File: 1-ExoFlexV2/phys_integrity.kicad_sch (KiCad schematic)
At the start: 18 parts, among them J112 Jumper, J113 Jumper, J114 Jumper, J115 Jumper, J116 Jumper, J117 Jumper, U88 OR Gate, U89 OR Gate, U90 OR Gate, U91 OR Gate, U92 OR Gate

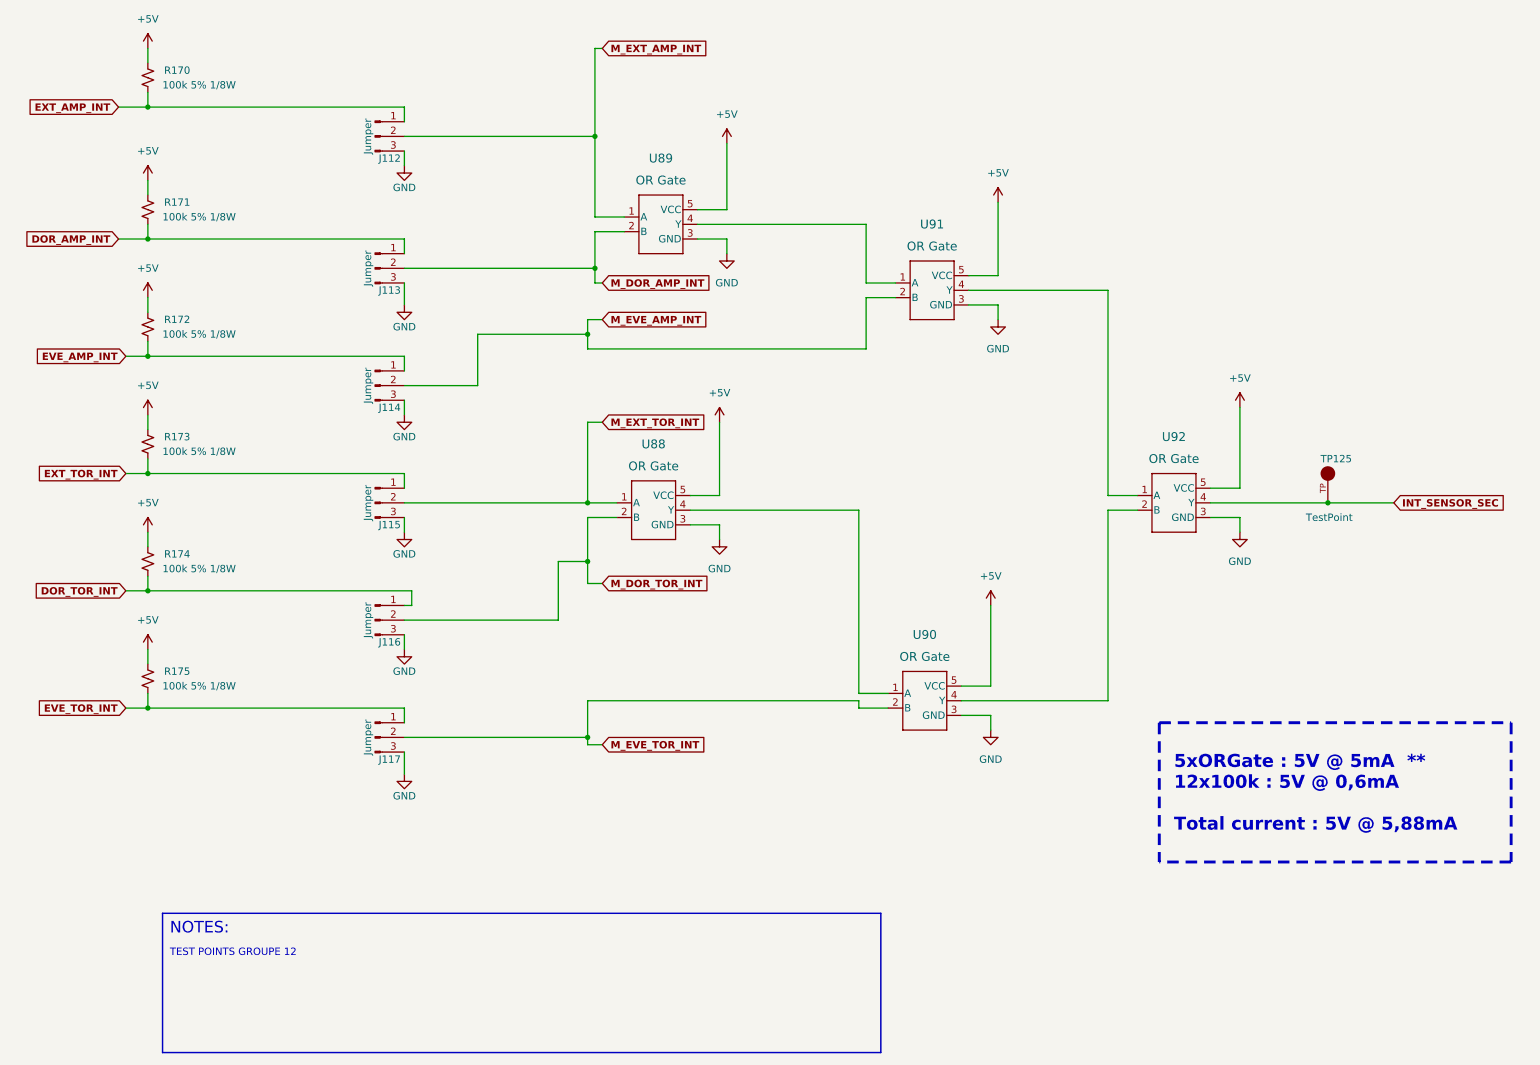
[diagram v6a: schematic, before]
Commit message: Finalisation schéma FIN
- Changement des uméro pour les inverseurs
- Changement des connecteur et début de placement
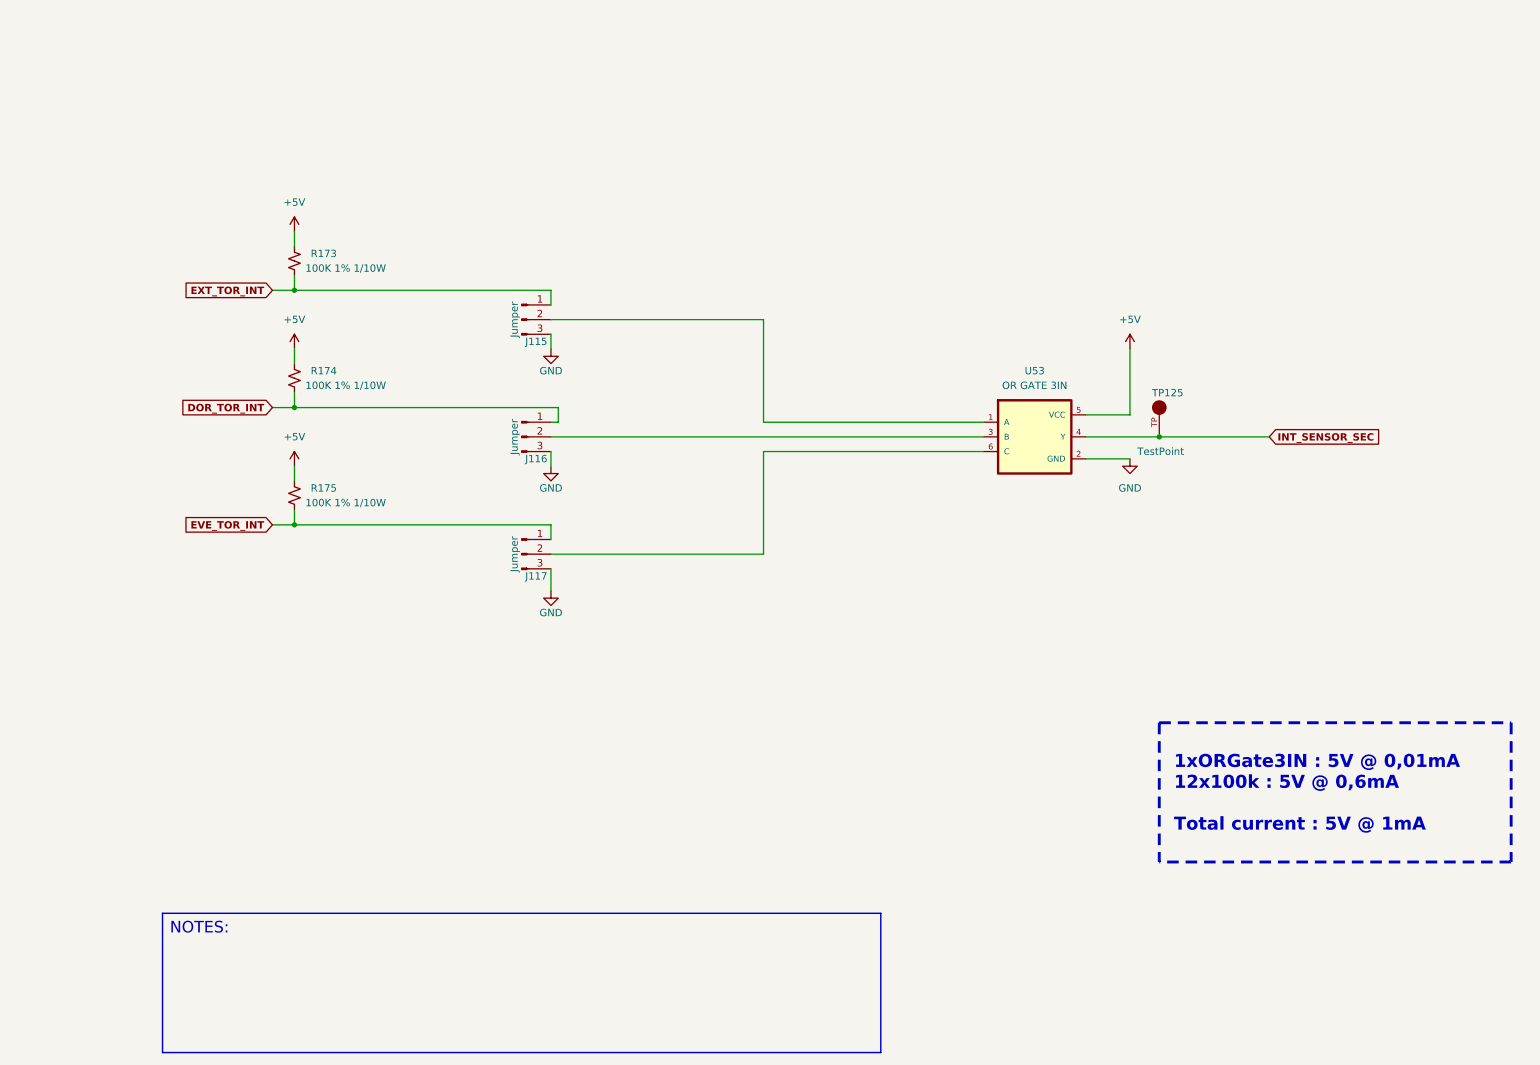
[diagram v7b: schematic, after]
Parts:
- removed J112, J113, J114: Jumper, Connector_PinHeader_2.54mm:PinHeader_1x03_P2.54mm_Vertical, symbol Connector:Conn_01x03_Male
- removed R170, R171, R172: 100k 5% 1/8W, Resistor_SMD:R_0805_2012Metric, symbol Device:R_Small_US
- removed U88, U89, U90, U91, U92: OR Gate, FootPrint:SOT95P270X145-5N, symbol SymLib:SN74LVC1G32DBVR
- added U53: OR GATE 3IN, FootPrintLib:SOT95P280X145-6N, symbol SymLib:SN74LVC1G332DBVR
- R173, R174, R175: value 100k 5% 1/8W -> 100K 1% 1/10W; footprint Resistor_SMD:R_0805_2012Metric -> Resistor_SMD:R_0603_1608Metric; DESCRIPTION 100 kOhms ±5% 0.125W, 1/8W Chip Resistor 0805 (2012 Metric)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 -> 100 kOhms ±1% 0.1W, 1/10W Chip Resistor 0603 (1608 Metric) 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; PACKAGE 0805 (2012 Metric) -> 0603 (1608 Metric); PART NUMBER ERJ-6GEYJ104V -> ERJ-3EKF1003V
- TP125: NOTES (none) -> DO NOT POPULATE; PURCHASE-URL https://pricing.snapeda.com/search/part/5005/?ref=eda -> (none)
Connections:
- net +5V: now also U53.5 (VCC)
- net GND: now also U53.2 (GND)
- net INT_SENSOR_SEC: now also U53.4 (Y)
- net M_DOR_TOR_INT: no longer names the net of J116.2 (Pin_2)
- net M_DOR_TOR_INT: now also U53.3 (B)
- net M_EVE_TOR_INT: no longer names the net of J117.2 (Pin_2)
- net M_EVE_TOR_INT: now also U53.6 (C)
- net M_EXT_TOR_INT: no longer names the net of J115.2 (Pin_2)
- net M_EXT_TOR_INT: now also U53.1 (A)
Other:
- note added: "1xORGate3IN : 5V @ 0,01mA 12x100k : 5V @ 0,6mA Total current : 5V @ 1mA"
- note removed: "5xORGate : 5V @ 5mA ** 12x100k : 5V @ 0,6mA Total current : 5V @ 5,88mA"
- note removed: "TEST POINTS GROUPE 12"
- moved on the sheet: J115, J116, J117, R173, R174, R175, TP125

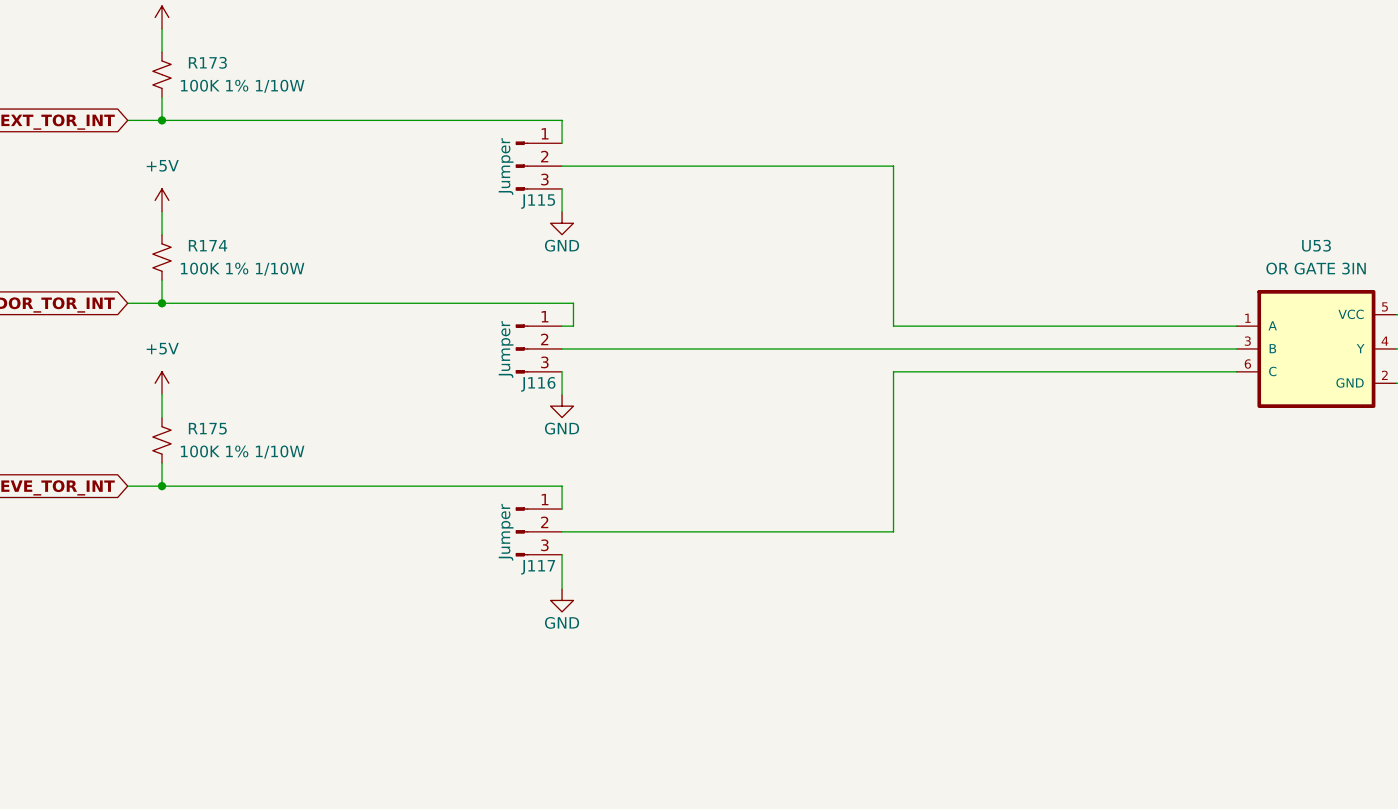
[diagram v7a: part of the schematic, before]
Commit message: Routage pour Review 1
- Replacement des test point pour faciliter le rework
- Correction des erreurs dans le BOM
-
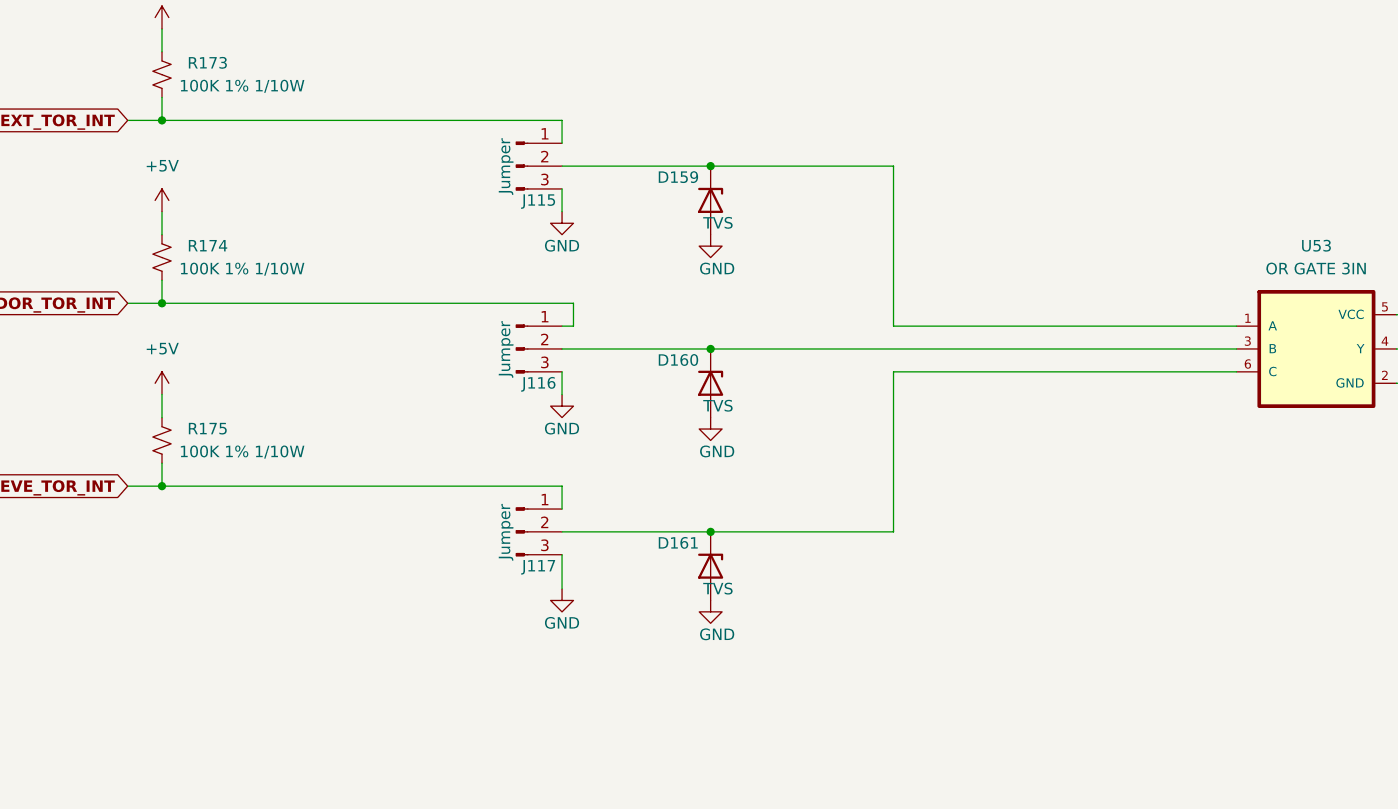
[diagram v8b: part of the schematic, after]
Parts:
- added D159, D160, D161: TVS, FootPrint:DPY2_TEX, symbol Device:D_Zener
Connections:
- net GND: now also D159.2 (A), D160.2 (A), D161.2 (A)
- net at J117.2 (Pin_2), U53.6 (C): now also D161.1 (K)
- net at J115.2 (Pin_2), U53.1 (A): now also D159.1 (K)
- net at J116.2 (Pin_2), U53.3 (B): now also D160.1 (K)
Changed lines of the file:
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@@
   (junction (at 71.12 102.87) (diameter 0) (color 0 0 0 0)
   )
+  (junction (at 132.08 107.95) (diameter 0) (color 0 0 0 0)
+  )
+  (junction (at 132.08 87.63) (diameter 0) (color 0 0 0 0)
+  )
+  (junction (at 132.08 67.31) (diameter 0) (color 0 0 0 0)
+  )
   (junction (at 71.12 62.23) (diameter 0) (color 0 0 0 0)
   )
@@
   )
   (wire (pts (xy 152.4 90.17) (xy 190.5 90.17))
+    (stroke (width 0) (type default) (color 0 0 0 0))
+  )
+  (wire (pts (xy 132.08 107.95) (xy 152.4 107.95))
     (stroke (width 0) (type default) (color 0 0 0 0))
   )
@@
     (stroke (width 0) (type default) (color 0 0 0 0))
   )
-  (wire (pts (xy 116.84 82.55) (xy 71.12 82.55))
+  (wire (pts (xy 71.12 82.55) (xy 116.84 82.55))
     (stroke (width 0) (type default) (color 0 0 0 0))
   )
@@
     (stroke (width 0) (type default) (color 0 0 0 0))
   )
-  (wire (pts (xy 115.57 87.63) (xy 190.5 87.63))
+  (wire (pts (xy 115.57 87.63) (xy 132.08 87.63))
     (stroke (width 0) (type default) (color 0 0 0 0))
   )
@@
     (stroke (width 0) (type default) (color 0 0 0 0))
   )
+  (wire (pts (xy 71.12 102.87) (xy 115.57 102.87))
+    (stroke (width 0) (type default) (color 0 0 0 0))
+  )
   (wire (pts (xy 71.12 52.07) (xy 71.12 54.61))
     (stroke (width 0) (type default) (color 0 0 0 0))
   )
-  (wire (pts (xy 71.12 102.87) (xy 115.57 102.87))
+  (wire (pts (xy 132.08 67.31) (xy 152.4 67.31))
     (stroke (width 0) (type default) (color 0 0 0 0))
   )
@@
     (stroke (width 0) (type default) (color 0 0 0 0))
   )
-  (wire (pts (xy 115.57 67.31) (xy 152.4 67.31))
+  (wire (pts (xy 132.08 87.63) (xy 190.5 87.63))
+    (stroke (width 0) (type default) (color 0 0 0 0))
+  )
+  (wire (pts (xy 115.57 67.31) (xy 132.08 67.31))
     (stroke (width 0) (type default) (color 0 0 0 0))
   )
@@
     (stroke (width 0) (type default) (color 0 0 0 0))
   )
-  (wire (pts (xy 115.57 107.95) (xy 152.4 107.95))
+  (wire (pts (xy 115.57 107.95) (xy 132.08 107.95))
     (stroke (width 0) (type default) (color 0 0 0 0))
   )
@@
     (pin "2")
   )
+  (symbol (lib_id "power:GND") (at 132.08 95.25 0) (unit 1)
+    (in_bom yes) (on_board yes)
+    (property "Reference" "#PWR0618" (id 0) (at 132.08 101.6 0)
+      (effects (font (size 1.27 1.27)) hide)
+    )
+    (property "Value" "GND" (id 1) (at 130.81 99.06 0)
+      (effects (font (size 1.27 1.27)) (justify left))
+    )
+    (property "Footprint" "" (id 2) (at 132.08 95.25 0)
+      (effects (font (size 1.27 1.27)) hide)
+    )
+    (property "Datasheet" "" (id 3) (at 132.08 95.25 0)
+      (effects (font (size 1.27 1.27)) hide)
+    )
+    (pin "1")
+  )
+  (symbol (lib_id "power:GND") (at 132.08 115.57 0) (unit 1)
+    (in_bom yes) (on_board yes)
+    (property "Reference" "#PWR0619" (id 0) (at 132.08 121.92 0)
+      (effects (font (size 1.27 1.27)) hide)
+    )
+    (property "Value" "GND" (id 1) (at 130.81 119.38 0)
+      (effects (font (size 1.27 1.27)) (justify left))
+    )
+    (property "Footprint" "" (id 2) (at 132.08 115.57 0)
+      (effects (font (size 1.27 1.27)) hide)
+    )
+    (property "Datasheet" "" (id 3) (at 132.08 115.57 0)
+      (effects (font (size 1.27 1.27)) hide)
+    )
+    (pin "1")
+  )
+  (symbol (lib_id "Device:D_Zener") (at 132.08 111.76 270) (unit 1)
+    (in_bom yes) (on_board yes)
+    (property "Reference" "D161" (id 0) (at 130.81 109.22 90)
+      (effects (font (size 1.27 1.27)) (justify right))
+    )
+    (property "Value" "TVS" (id 1) (at 134.62 114.3 90)
+      (effects (font (size 1.27 1.27)) (justify right))
+    )
+    (property "Footprint" "FootPrint:DPY2_TEX" (id 2) (at 132.08 111.76 0)
+      (effects (font (size 1.27 1.27)) hide)
+    )
+    (property "Datasheet" "~" (id 3) (at 132.08 111.76 0)
+      (effects (font (size 1.27 1.27)) hide)
+    )
+    (property "DESCRIPTION" "TVS DIODE 5.5VWM 14VC 2X1SON" (id 4) (at 132.08 111.76 0)
+      (effects (font (size 1.27 1.27)) hide)
+    )
+    (property "MANUFACTURER" "Texas Instruments" (id 5) (at 132.08 111.76 0)
+      (effects (font (size 1.27 1.27)) hide)
+    )
+    (property "PACKAGE" "0402 (1006 Metric)" (id 6) (at 132.08 111.76 0)
+      (effects (font (size 1.27 1.27)) hide)
+    )
+    (property "PART NUMBER" "TPD1E05U06DPYR" (id 7) (at 132.08 111.76 0)
+      (effects (font (size 1.27 1.27)) hide)
+    )
+    (property "TYPE" "SMD" (id 8) (at 132.08 111.76 0)
+      (effects (font (size 1.27 1.27)) hide)
+    )
+    (pin "1")
+    (pin "2")
+  )
   (symbol (lib_id "Device:R_Small_US") (at 71.12 77.47 0) (unit 1)
     (in_bom yes) (on_board yes)
@@
     )
     (pin "1")
+  )
+  (symbol (lib_id "Device:D_Zener") (at 132.08 91.44 270) (unit 1)
+    (in_bom yes) (on_board yes)
+    (property "Reference" "D160" (id 0) (at 130.81 88.9 90)
+      (effects (font (size 1.27 1.27)) (justify right))
+    )
+    (property "Value" "TVS" (id 1) (at 134.62 93.98 90)
+      (effects (font (size 1.27 1.27)) (justify right))
+    )
+    (property "Footprint" "FootPrint:DPY2_TEX" (id 2) (at 132.08 91.44 0)
+      (effects (font (size 1.27 1.27)) hide)
+    )
+    (property "Datasheet" "~" (id 3) (at 132.08 91.44 0)
+      (effects (font (size 1.27 1.27)) hide)
+    )
+    (property "DESCRIPTION" "TVS DIODE 5.5VWM 14VC 2X1SON" (id 4) (at 132.08 91.44 0)
+      (effects (font (size 1.27 1.27)) hide)
+    )
+    (property "MANUFACTURER" "Texas Instruments" (id 5) (at 132.08 91.44 0)
+      (effects (font (size 1.27 1.27)) hide)
+    )
+    (property "PACKAGE" "0402 (1006 Metric)" (id 6) (at 132.08 91.44 0)
+      (effects (font (size 1.27 1.27)) hide)
+    )
+    (property "PART NUMBER" "TPD1E05U06DPYR" (id 7) (at 132.08 91.44 0)
+      (effects (font (size 1.27 1.27)) hide)
+    )
+    (property "TYPE" "SMD" (id 8) (at 132.08 91.44 0)
+      (effects (font (size 1.27 1.27)) hide)
+    )
+    (pin "1")
+    (pin "2")
   )
   (symbol (lib_id "SymLib:SN74LVC1G332DBVR") (at 199.39 92.71 0) (unit 1)
@@
     (pin "6")
   )
+  (symbol (lib_id "Device:D_Zener") (at 132.08 71.12 270) (unit 1)
+    (in_bom yes) (on_board yes)
+    (property "Reference" "D159" (id 0) (at 130.81 68.58 90)
+      (effects (font (size 1.27 1.27)) (justify right))
+    )
+    (property "Value" "TVS" (id 1) (at 134.62 73.66 90)
+      (effects (font (size 1.27 1.27)) (justify right))
+    )
+    (property "Footprint" "FootPrint:DPY2_TEX" (id 2) (at 132.08 71.12 0)
+      (effects (font (size 1.27 1.27)) hide)
+    )
+    (property "Datasheet" "~" (id 3) (at 132.08 71.12 0)
+      (effects (font (size 1.27 1.27)) hide)
+    )
+    (property "DESCRIPTION" "TVS DIODE 5.5VWM 14VC 2X1SON" (id 4) (at 132.08 71.12 0)
+      (effects (font (size 1.27 1.27)) hide)
+    )
+    (property "MANUFACTURER" "Texas Instruments" (id 5) (at 132.08 71.12 0)
+      (effects (font (size 1.27 1.27)) hide)
+    )
+    (property "PACKAGE" "0402 (1006 Metric)" (id 6) (at 132.08 71.12 0)
+      (effects (font (size 1.27 1.27)) hide)
+    )
+    (property "PART NUMBER" "TPD1E05U06DPYR" (id 7) (at 132.08 71.12 0)
+      (effects (font (size 1.27 1.27)) hide)
+    )
+    (property "TYPE" "SMD" (id 8) (at 132.08 71.12 0)
+      (effects (font (size 1.27 1.27)) hide)
+    )
+    (pin "1")
+    (pin "2")
+  )
   (symbol (lib_id "Device:R_Small_US") (at 71.12 57.15 0) (unit 1)
     (in_bom yes) (on_board yes)
@@
       (effects (font (size 1.27 1.27)) hide)
     )
+    (pin "1")
+  )
+  (symbol (lib_id "power:GND") (at 132.08 74.93 0) (unit 1)
+    (in_bom yes) (on_board yes)
+    (property "Reference" "#PWR0617" (id 0) (at 132.08 81.28 0)
+      (effects (font (size 1.27 1.27)) hide)
+    )
+    (property "Value" "GND" (id 1) (at 130.81 78.74 0)
+      (effects (font (size 1.27 1.27)) (justify left))
+    )
+    (property "Footprint" "" (id 2) (at 132.08 74.93 0)
+      (effects (font (size 1.27 1.27)) hide)
+    )
+    (property "Datasheet" "" (id 3) (at 132.08 74.93 0)
+      (effects (font (size 1.27 1.27)) hide)
+    )
